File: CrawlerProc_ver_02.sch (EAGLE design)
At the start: 57 parts, among them U1 MIC5335-SPYMT, U10 ECS-160-8, U11 ANTENNA, U12 ANTENNA-CHIP, U2 MIC5320-JGYML, U3 ITG-3200, U4 AT86RF231-ZU, U5 AT45DB321D, U6 ECS-2033, U8 ADXL345-LGA12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

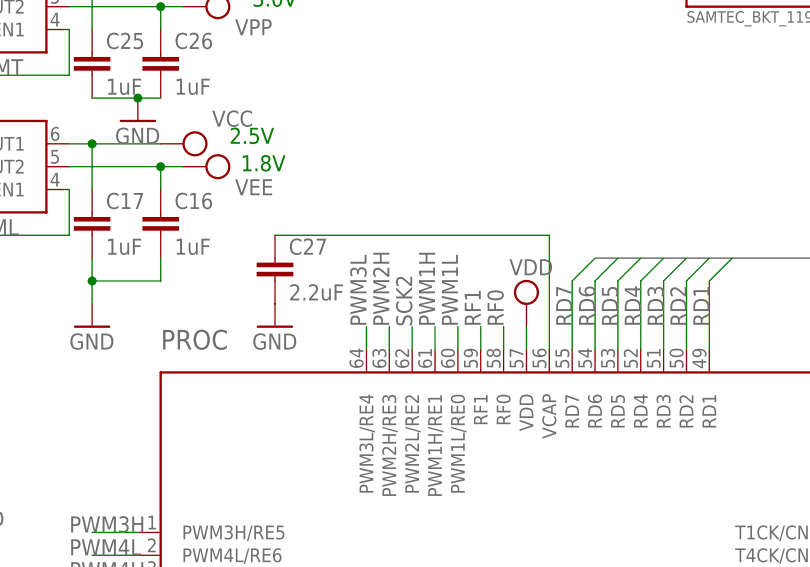
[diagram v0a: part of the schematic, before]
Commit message: Fixed error that connected PWM2L to the SCK2 line
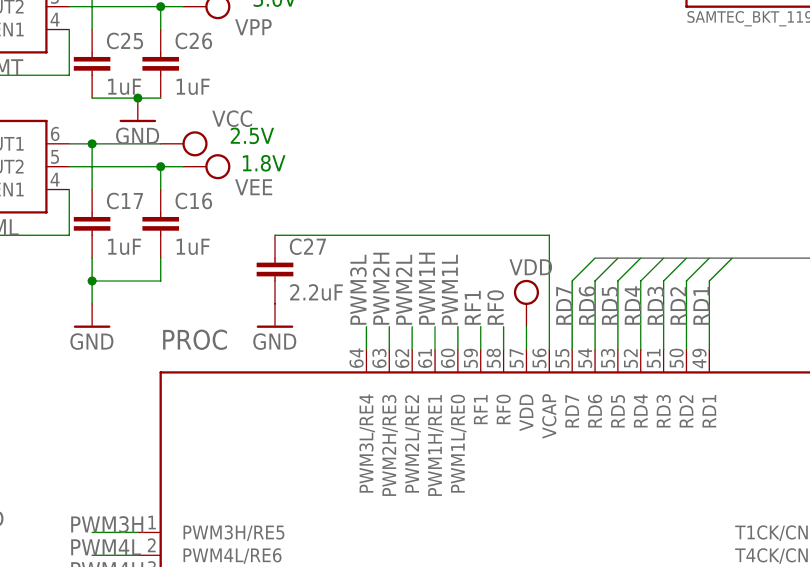
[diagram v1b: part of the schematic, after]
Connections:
- new net PWM2L: PROC.PWM2L/RE2
- net SCK2: no longer PROC.PWM2L/RE2
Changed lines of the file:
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@@
 <net name="SCK2" class="0">
-<segment>
-<wire x1="99.06" y1="124.46" x2="99.06" y2="127" width="0.1524" layer="91"/>
-<label x="99.06" y="127" size="1.778" layer="95" rot="R90"/>
-<pinref part="PROC" gate="G$1" pin="PWM2L/RE2"/>
-</segment>
 <segment>
 <wire x1="127" y1="187.96" x2="124.46" y2="187.96" width="0.2032" layer="91"/>
@@
 </segment>
 </net>
+<net name="PWM2L" class="0">
+<segment>
+<wire x1="99.06" y1="124.46" x2="99.06" y2="127" width="0.1524" layer="91"/>
+<label x="99.06" y="127" size="1.778" layer="95" rot="R90"/>
+<pinref part="PROC" gate="G$1" pin="PWM2L/RE2"/>
+</segment>
+</net>
